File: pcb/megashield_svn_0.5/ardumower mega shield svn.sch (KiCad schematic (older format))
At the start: 99 parts, among them K1 Tilt sens, K2 Button, K3 RELAY_2RT, P1 Sonar C, P10 GPS, P11 Bumper, P12 PerimeterRight, P13 RC Remote, P15 Dual2-M1Out, P16 Dual2-pwr, P17 Dual1-pwr, P18 Mow Motor, P19 DS1307, P2 Sonar R, P20 Wlan, P21 DropRight, P22 CONN_01X01, P23 CONN_01X01, P24 CONN_01X01, P25 CONN_01X01, P26 CONN_01X01, P27 CONN_01X01, P28 CONN_01X01, P29 CONN_01X01, P3 Sonar L, P30 PerimeterRight, P31 DropLeft, P32 Stromleiste GND, P33 Stromleiste 5V, P34 Stromleiste 3,3V, P35 MowRpm, P40 UserSwitsch, P41 Rain, P5 IMU Kompas, P6 Lawn sens, P7 Status LEDs, P8 ODO Right, P9 ODO Left, Q1 BC237, U1 DC-DC, U2 HC05_Bluetooth, U3 INA169 Adafruit, U4 LM350T, U5 INA169 Adafruit

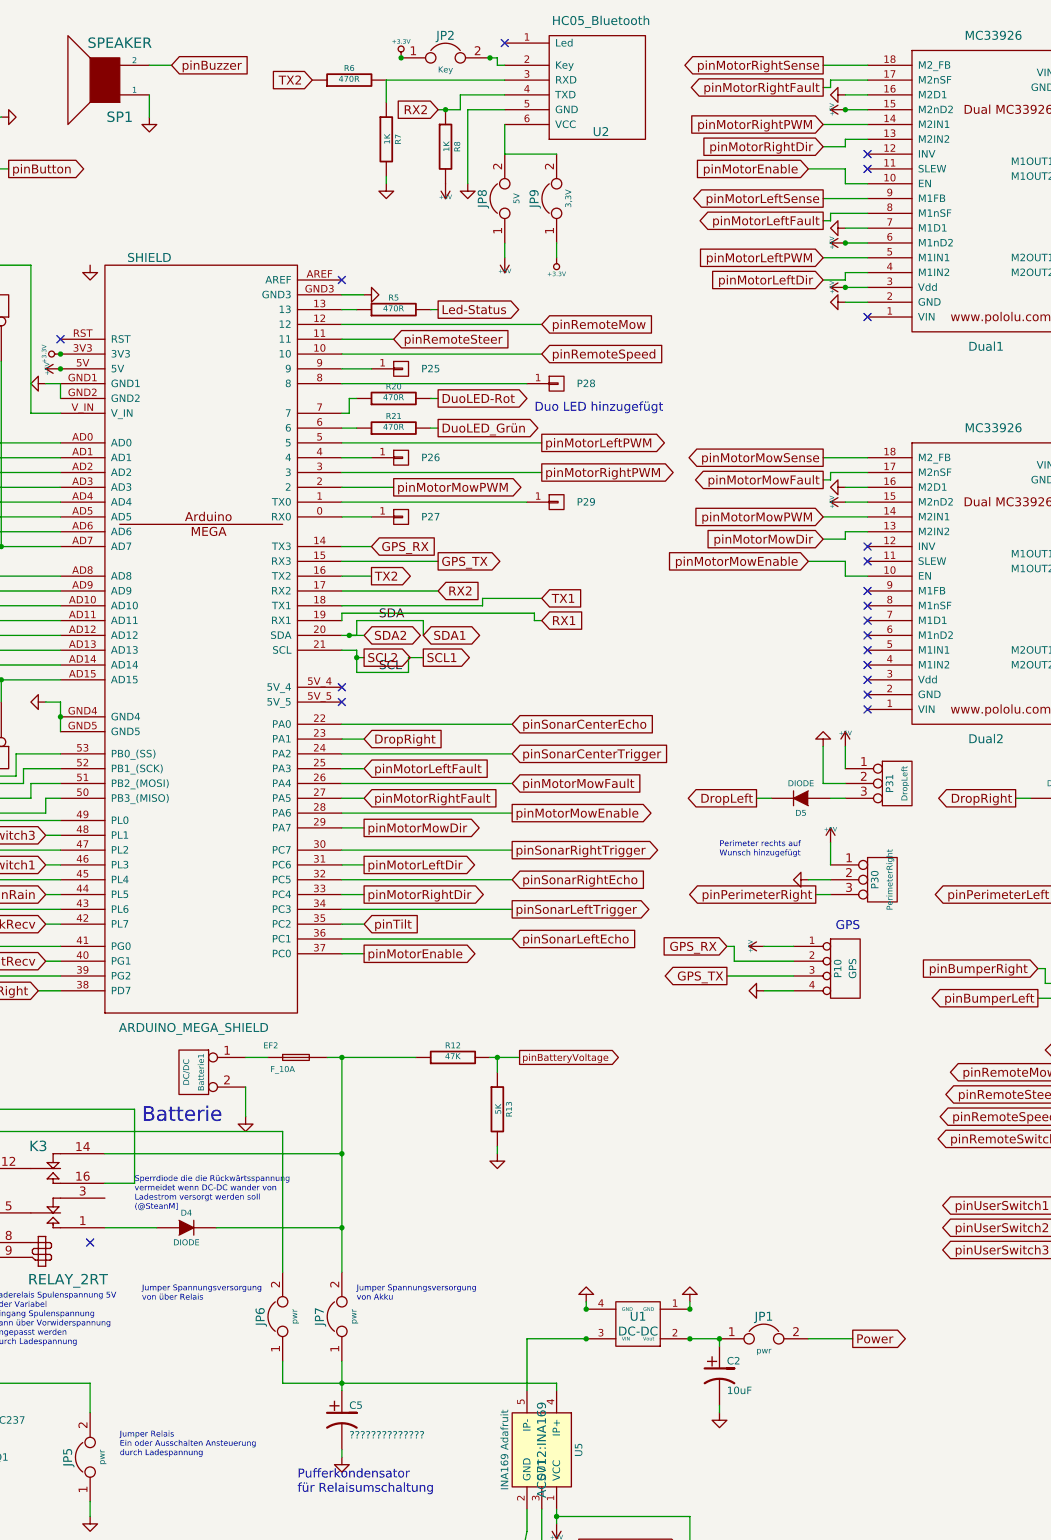
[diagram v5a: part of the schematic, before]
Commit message: zusätzliche Spannungsversorgung
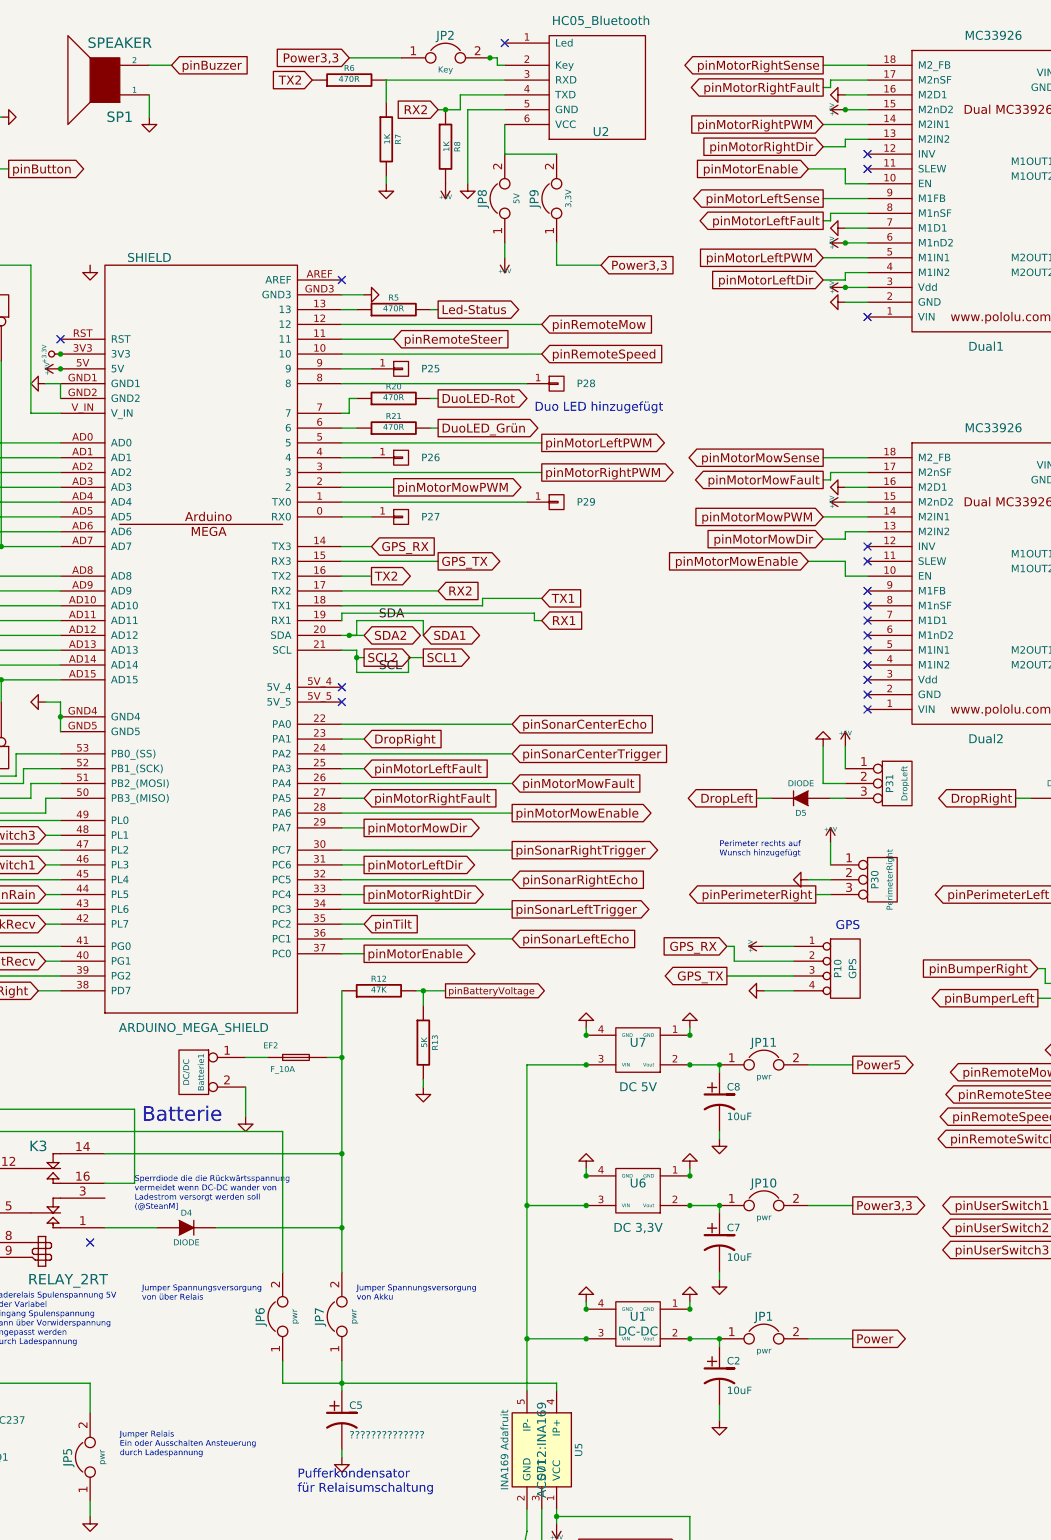
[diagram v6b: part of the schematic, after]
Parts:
- added C7, C8: 10uF, Capacitors_ThroughHole:Capacitor3MMDiscRM2.5, symbol CP1
- added JP10, JP11: pwr, Pin_Headers:Pin_Header_Straight_1x02, symbol JUMPER
- added U6: DC 3,3V, ACS712:DC-DC, symbol DC-DC_Stepdown
- added U7: DC 5V, ACS712:DC-DC, symbol DC-DC_Stepdown
- JP7: footprint Pin_Headers:Pin_Header_Straight_1x02 -> Pin_Headers:Pin_Header_Straight_1x03
- K3: footprint ACS712:Relais_DPDT_Schrack-RT2_RM5mm -> Relays_ThroughHole:Relais_DPDT_Schrack-RT2_RM5mm
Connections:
- net +3.3V: no longer JP2.1, JP9.1
- net GND: now also C7.2, C8.2, U6.1 (GND), U6.4 (GND), U7.1 (GND), U7.4 (GND)
- net at U1.3 (VIN), U5.5 (IP-): now also U6.3 (VIN), U7.3 (VIN)
- new net: C7.1, JP10.1, U6.2 (Vout)
- new net: C8.1, JP11.1, U7.2 (Vout)
- new net Power3,3: JP10.2, JP2.1, JP9.1
- new net Power5: JP11.2
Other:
- moved on the sheet: R12, R13

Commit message: Platinenlayout weiter gearbeitet
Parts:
- added JP12: pwr, Pin_Headers:Pin_Header_Straight_1x02, symbol JUMPER
- U1: value DC-DC -> DC 10V
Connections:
- net Power5 is gone; now on net +5V: JP11.2
- net +5V: now also JP12.1; no longer SHIELD1.5V
- new net: JP12.2, SHIELD1.5V

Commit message: Platinenlayout weiter gearbeitet
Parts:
- removed P22, P23, P24, P25, P26, P27, P28, P29: CONN_01X01, Pin_Headers:Pin_Header_Straight_1x01, symbol CONN_01X01
- added P14: ReserveAD7, Pin_Headers:Pin_Header_Straight_1x03, symbol CONN_3
- added P22: ReserveAD6, Pin_Headers:Pin_Header_Straight_1x03, symbol CONN_3
- added P23: I2C Res.1, Pin_Headers:Pin_Header_Straight_1x05, symbol CONN_5
- added P24: I2C Res.2, Pin_Headers:Pin_Header_Straight_1x05, symbol CONN_5
- added P25: ReservePin9, Pin_Headers:Pin_Header_Straight_1x03, symbol CONN_3
- added P26: ReservePin4, Pin_Headers:Pin_Header_Straight_1x03, symbol CONN_3
- added P27: ReservePin0, Pin_Headers:Pin_Header_Straight_1x03, symbol CONN_3
- added P28: ReservePin8, Pin_Headers:Pin_Header_Straight_1x03, symbol CONN_3
- added P29: ReservePin1, Pin_Headers:Pin_Header_Straight_1x03, symbol CONN_3
- added P4: ReserveAD11, Pin_Headers:Pin_Header_Straight_1x03, symbol CONN_3
- JP7: footprint Pin_Headers:Pin_Header_Straight_1x03 -> Pin_Headers:Pin_Header_Straight_1x02
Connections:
- net Power3,3 is gone; now on net +3.3V: JP10.2, JP2.1, JP9.1
- net +3.3V: no longer SHIELD1.3V3
- net +5V: now also P19.2, P14.1 (P1), P22.1 (P1), P23.1, P24.1, P25.1 (P1), P26.1 (P1), P27.1 (P1), P28.1 (P1), P29.1 (P1), P4.1 (P1); no longer P19.1
- net GND: now also P10.2 (P2), P19.1, P14.2 (PM), P22.2 (PM), P23.2, P24.2, P25.2 (PM), P26.2 (PM), P27.2 (PM), P28.2 (PM), P29.2 (PM), P4.2 (PM); no longer P10.4 (P4), P19.2
- net GPS_RX: now also P10.3 (P3); no longer P10.2 (P2)
- net GPS_TX: now also P10.4 (P4); no longer P10.3 (P3)
- net SCL1: now also P23.4, P24.4
- net SDA1: now also P23.3, P24.3
- net ReservePin0: now reaches SHIELD1.0 (RX0)
- net ReservePin0: now also P27.3 (P3)
- net ReservePin1: now reaches SHIELD1.1 (TX0)
- net ReservePin1: now also P29.3 (P3)
- net ReservePin4: now reaches SHIELD1.4
- net ReservePin4: now also P26.3 (P3)
- net ReservePin8: now reaches SHIELD1.8
- net ReservePin8: now also P28.3 (P3)
- net ReservePin9: now reaches SHIELD1.9
- net ReservePin9: now also P25.3 (P3)
- net ReserveAD7: now reaches RP1.1 (P1)
- net ReserveAD7: now also P14.3 (P3)
- net ReserveAD6: now reaches RP1.2 (P2)
- net ReserveAD6: now also P22.3 (P3)
- net ReserveAD11: now reaches RP2.5 (P5)
- net ReserveAD11: now also P4.3 (P3)
- no-connect marks 35 -> 38
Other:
- moved on the sheet: JP12, P35
